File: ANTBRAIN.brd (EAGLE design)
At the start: 40 x 40 mm, 26 parts, among them IC1 ATMEGA328P, SW1 SWITCH-SPDTB

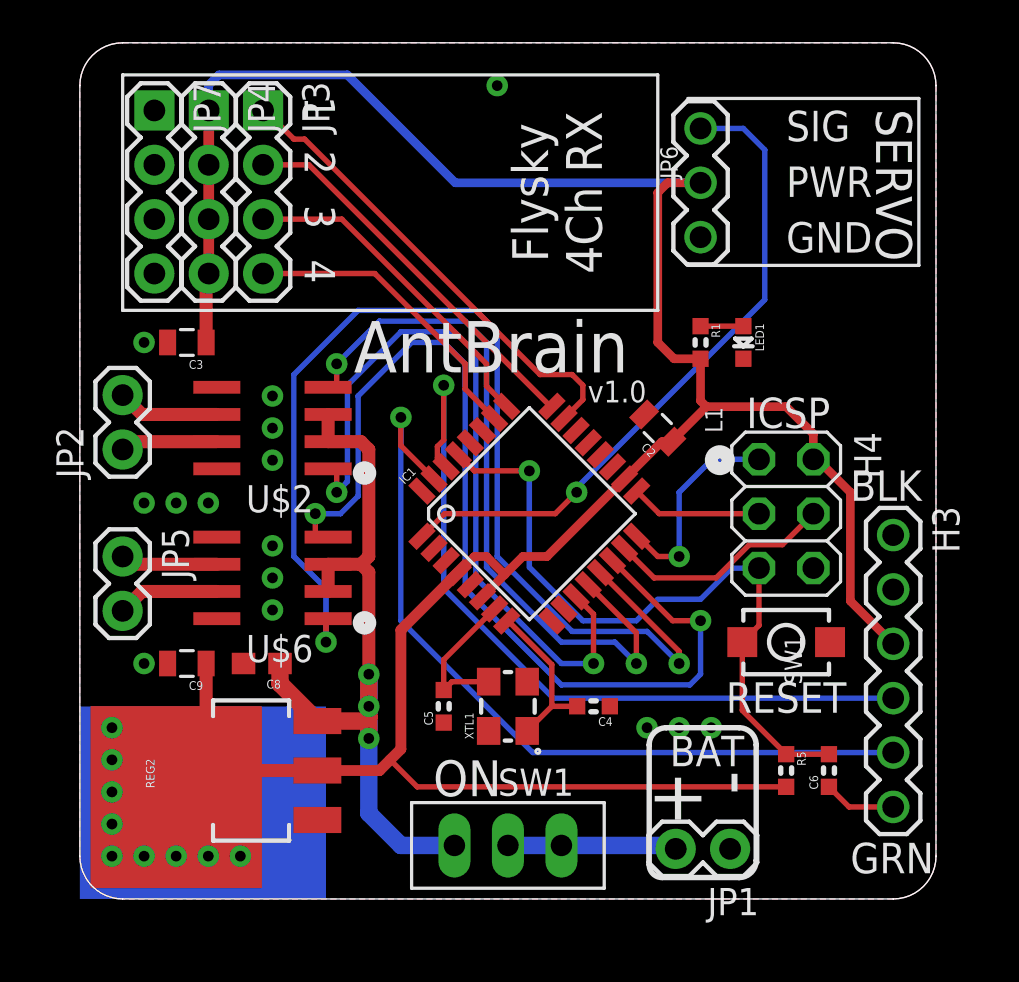
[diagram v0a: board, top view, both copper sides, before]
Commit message: Shrunk board to 36x36mm
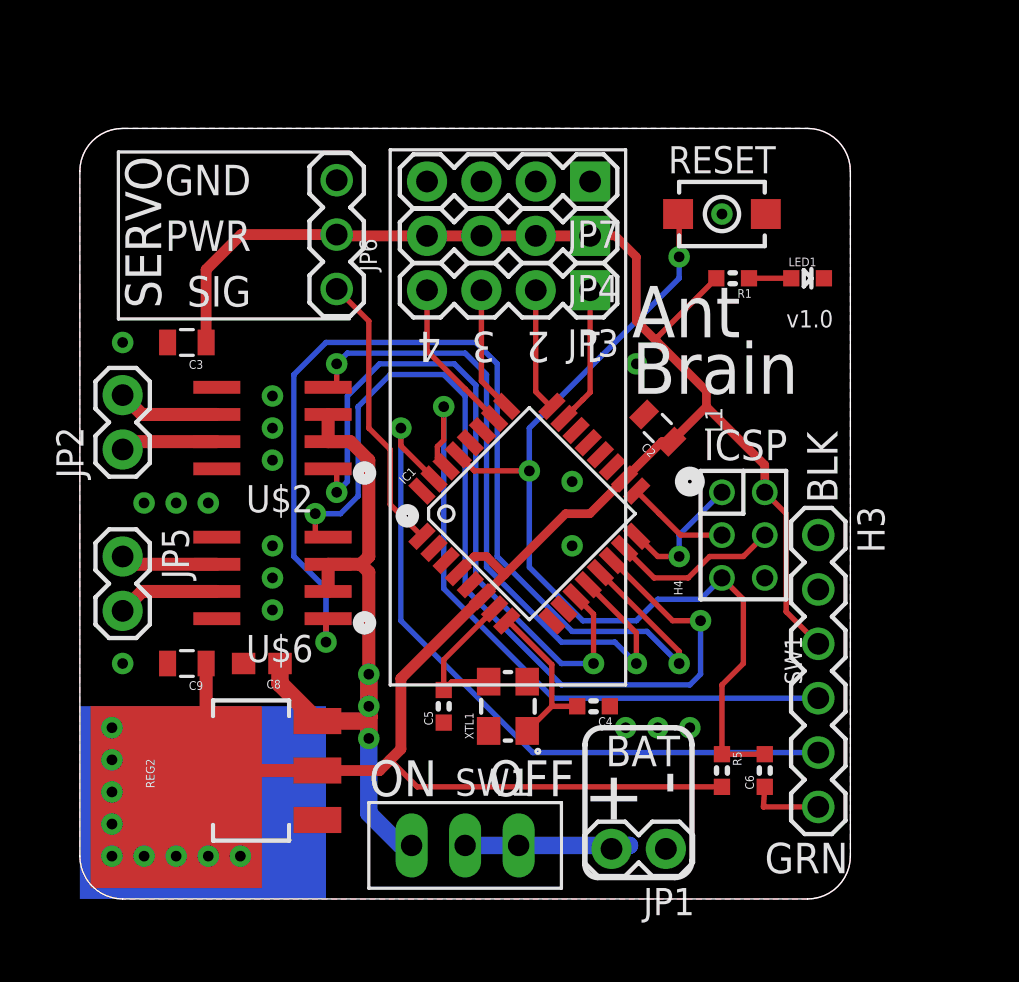
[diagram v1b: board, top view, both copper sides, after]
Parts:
- H4: value ICSP -> ICSP2X3-2MM; device pinhead:2X03 -> freetronics-jon:M2X3-2MM
- moved JP7 20.6 mm to (23.8, 33.5), turned to 180 degrees
- moved S1 20.2 mm to (30.0, 32.0)
- moved JP4 18.8 mm to (23.8, 31.0), turned to 180 degrees
- moved JP6 18.6 mm to (12.0, 28.5), turned to 90 degrees
- moved JP3 17.4 mm to (23.8, 28.4), turned to 180 degrees
- moved LED1 4.24 mm to (34.0, 29.0), turned to 0 degrees
- moved H3 3.50 mm to (34.5, 17.0)
- moved R1 3.35 mm to (30.5, 29.0), turned to 180 degrees
- moved C6 3.00 mm to (32.0, 6.00)
- moved JP1 3.00 mm to (27.4, 2.34)
- moved R5 3.00 mm to (30.0, 6.00)
- moved H4 2.24 mm to (31.0, 17.0), turned to 90 degrees
- moved SW1 2.00 mm to (18.0, 2.50)
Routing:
- net 5V: track 145.1 -> 123.7 mm
- net D3: track 31.4 -> 13.2 mm, vias 1 -> 0
- net A0: track 22.2 -> 6.60 mm
- net A1: track 18.2 -> 5.78 mm
- net RESET: track 32.8 -> 45.0 mm, vias 1 -> 2
- net A2: track 15.6 -> 5.92 mm
- net A3: track 14.3 -> 7.30 mm
- net D0_RX: track 36.7 -> 31.2 mm
- net D1_TX: track 38.6 -> 34.1 mm
- net D12_MISO: track 9.74 -> 6.20 mm
- net D11_MOSI: track 10.6 -> 7.95 mm
- net D7: track 35.4 -> 33.0 mm
- net D10: track 46.4 -> 44.0 mm
- net VBAT: track 37.7 -> 35.4 mm
- net D9: track 52.5 -> 50.3 mm
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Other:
- board size 40 x 40 mm -> 36 x 36 mm
- board text added: "Ant Brain"
- board text added: "OFF"
- board text removed: "Flysky 4Ch RX"

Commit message: Finished routing for v1.0 release
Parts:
- removed U$2, U$6: L9110SO8, freetronics-jon:SO08
- added IC2, IC3: L9110SO8, freetronics-jon:SO08
- added JP10: POWER, freetronics-jon:M02-2MM
- added JP8: (no value), freetronics-jon:M02-2MM
- added JP9: D13, freetronics-jon:M02-2MM
- added LED2: RED, freetronics-jon:LED-0603
- added R2, R3: 10K, freetronics-jon:0603
- added R4: 1K, freetronics-jon:0603
- added R6, R7: 470R, freetronics-jon:0603
- moved LED1 28.4 mm to (6.00, 33.5), turned to 90 degrees
- moved JP1 28.2 mm to (33.7, 29.9), turned to 270 degrees
- moved S1 27.0 mm to (3.00, 31.5), turned to 90 degrees
- moved R5 26.6 mm to (24.5, 32.0), turned to 0 degrees
- moved C6 25.6 mm to (24.5, 30.5), turned to 180 degrees
- moved C2 25.0 mm to (2.50, 27.0), turned to 180 degrees
- moved R1 24.5 mm to (6.00, 30.0), turned to 270 degrees
- moved JP7 23.5 mm to (2.48, 23.8), turned to 270 degrees
- moved H3 23.4 mm to (19.0, 34.5), turned to 0 degrees
- moved SW1 23.4 mm to (33.5, 20.0), turned to 270 degrees
- moved JP2 23.0 mm to (15.0, 2.00), turned to 180 degrees
- moved JP5 22.8 mm to (20.0, 2.00), turned to 0 degrees
- moved REG2 22.1 mm to (30.0, 8.00), turned to 180 degrees
- moved C3 22.0 mm to (9.50, 4.50), turned to 270 degrees
- moved C9 21.5 mm to (25.5, 4.50), turned to 90 degrees
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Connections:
- removed net N$1: JP2.1, U$2.7
- removed net N$2: JP2.2, U$2.6
- removed net N$3: JP5.2, U$6.7
- removed net N$4: JP5.1, U$6.6
- new net LA: IC2.6, JP2.2
- new net LB: IC2.7, JP2.1
- new net N$5: LED2.A, R4.1
- new net N$6: JP10.1, R7.1
- new net N$8: JP9.1, R6.1
- new net RA: IC3.6, JP5.1
- new net RB: IC3.7, JP5.2
- net 5V: now also R7.2
- net A6: now also R2.2, R3.1
- net D10: now also IC3.4; no longer U$6.4
- net D13_SCK: now also R4.2, R6.2
- net D7: now also IC2.1; no longer U$2.1
- net D8: now also IC2.4; no longer U$2.4
- net D9: now also IC3.1; no longer U$6.1
- net GND: now also IC2.5, IC2.8, IC3.5, IC3.8, JP10.2, JP9.2, LED2.C, R2.1; no longer U$2.5, U$2.8, U$6.5, U$6.8
- net N$9: now also JP8.2
- net VBAT: now also IC2.2, IC2.3, IC3.2, IC3.3, JP8.1, R3.2; no longer U$2.2, U$2.3, U$6.2, U$6.3
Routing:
- net A6: track 0.00 -> 55.4 mm, vias 0 -> 2
- net D13_SCK: track 4.84 -> 22.5 mm, vias 0 -> 2
- net VBAT: track 35.4 -> 48.7 mm
- net RTS: track 3.50 -> 9.60 mm
- net N$3: track 4.77 -> 0.00 mm
- net LA: track 0.00 -> 4.77 mm
- net RB: track 0.00 -> 4.77 mm
- net N$2: track 4.77 -> 0.00 mm
- net N$4: track 4.55 -> 0.00 mm
- net LB: track 0.00 -> 4.55 mm
- net RA: track 0.00 -> 4.55 mm
- net N$1: track 4.55 -> 0.00 mm
- net 5V: track 123.7 -> 120.2 mm
- net N$9: track 8.54 -> 10.5 mm
- net N$5: track 0.00 -> 1.98 mm
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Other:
- board text added: "BK"
- board text added: "D13"
- board text added: "LA"
- board text added: "LB"
- board text added: "RA"
- board text added: "RB"
- board text added: "SWITCH"
- board text added: "freetronics"
- board text removed: "Ant Brain"
- board text removed: "BLK"
- board text removed: "OFF"

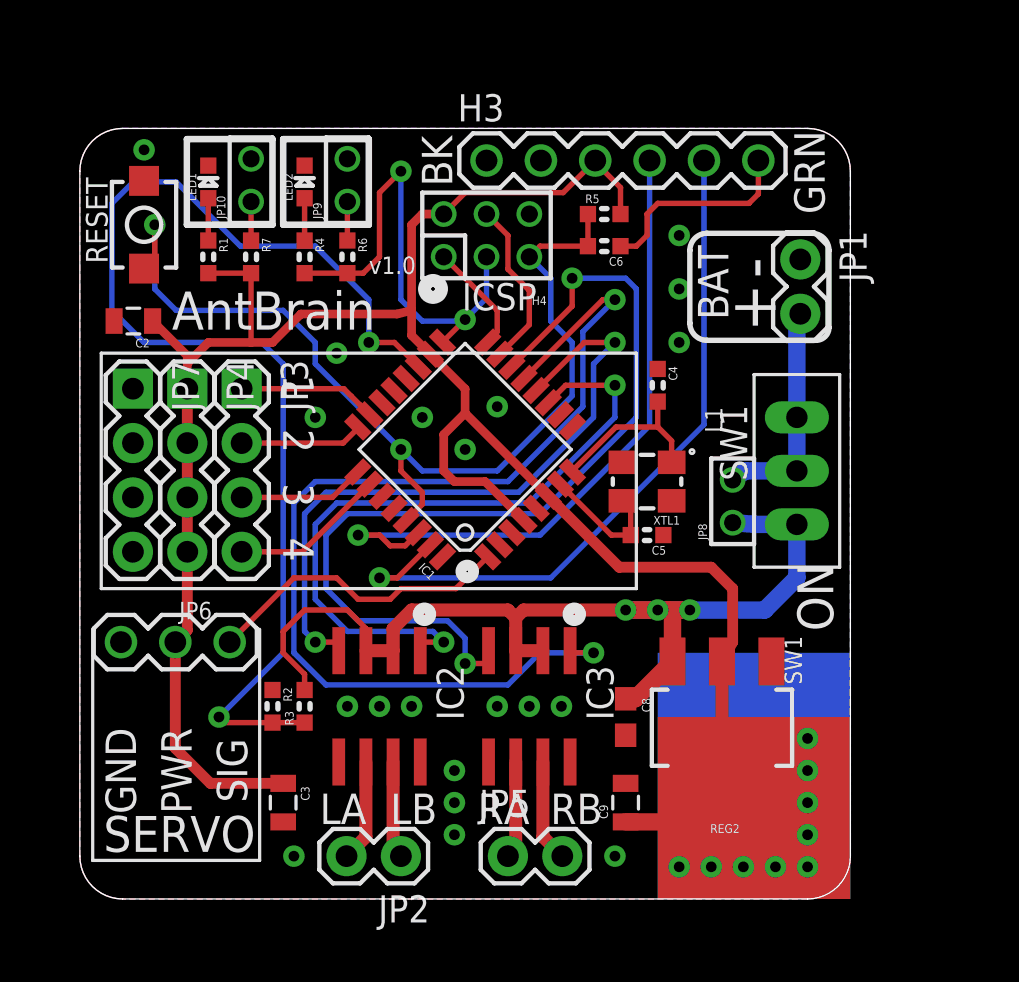
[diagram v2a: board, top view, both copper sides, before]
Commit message: Fixed H-Bridge footprints for v1.1 release
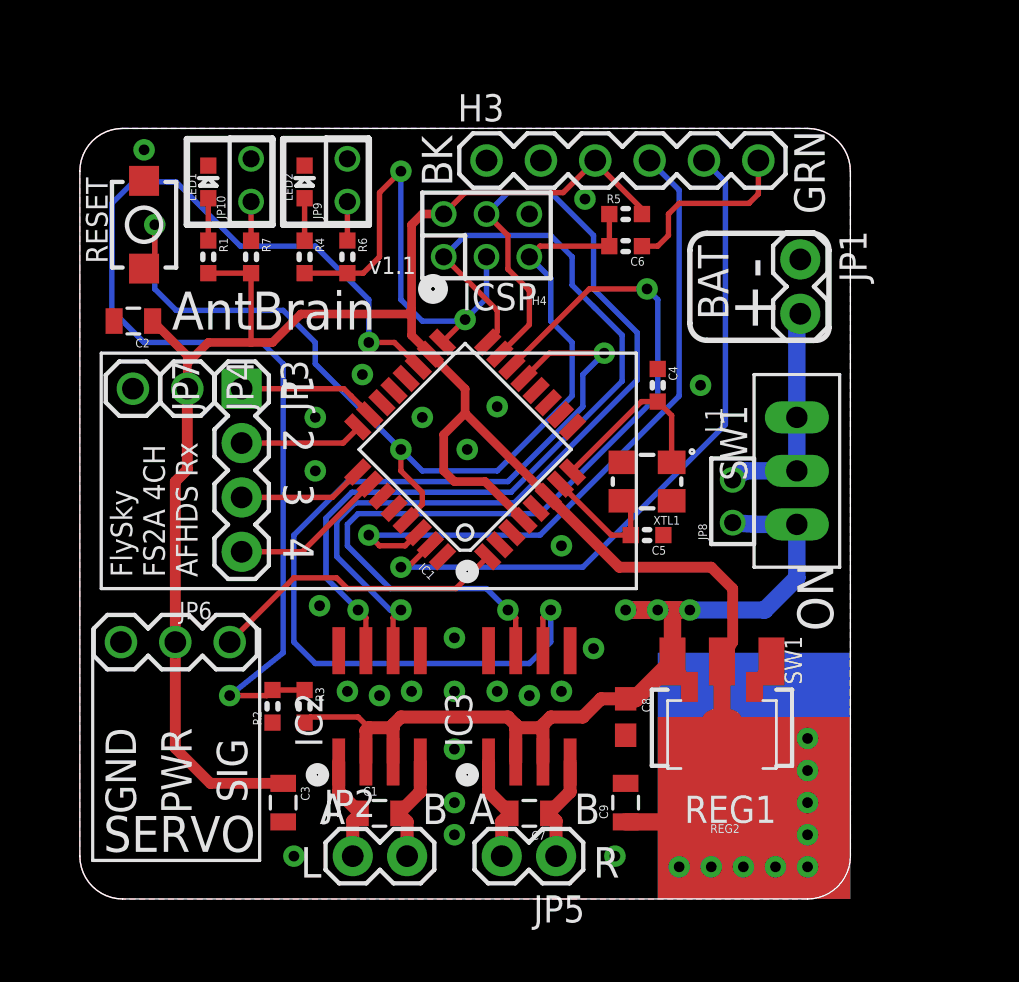
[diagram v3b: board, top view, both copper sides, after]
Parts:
- added C1, C7: 10uF, freetronics-jon:0805
- added REG1: LD1117-SOT89, freetronics:SOT89
- JP4, JP7: value (none) -> M01PTH; device freetronics-jon:1X04 -> freetronics-jon:1X01
- moved JP2 2.25 mm to (12.8, 2.00), turned to 0 degrees
- moved JP5 2.25 mm to (22.2, 2.00), turned to 180 degrees
- moved C6 1.00 mm to (25.5, 30.5)
- moved R5 1.00 mm to (25.5, 32.0)
- turned IC2 to 0 degrees
- turned IC3 to 0 degrees
- turned R2 to 90 degrees
- turned R3 to 270 degrees
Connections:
- removed net LA: IC2.6, JP2.2
- removed net LB: IC2.7, JP2.1
- removed net RA: IC3.6, JP5.1
- removed net RB: IC3.7, JP5.2
- new net LOA: C1.1, IC2.1, JP2.1
- new net LOB: C1.2, IC2.4, JP2.2
- new net ROA: C7.2, IC3.1, JP5.2
- new net ROB: C7.1, IC3.4, JP5.1
- net 5V: now also REG1.2, REG1.4; no longer JP4.2, JP4.3, JP4.4
- net D10: now also IC3.7; no longer IC3.4
- net D11_MOSI: now also IC2.6
- net D12_MISO: now also IC2.7
- net D7: no longer IC2.1
- net D8: no longer IC2.4
- net D9: now also IC3.6; no longer IC3.1
- net GND: now also REG1.1; no longer JP7.2, JP7.3, JP7.4
- net VBAT: now also REG1.3
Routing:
- net D11_MOSI: track 7.95 -> 46.3 mm, vias 0 -> 1
- net D12_MISO: track 5.20 -> 42.3 mm, vias 0 -> 1
- net D7: track 33.0 -> 0.00 mm, vias 2 -> 0
- net D8: track 31.5 -> 0.00 mm, vias 2 -> 0
- net D9: track 50.3 -> 44.5 mm
- net ROA: track 0.00 -> 4.98 mm
- net LOB: track 0.00 -> 4.98 mm
- net ROB: track 0.00 -> 4.96 mm
- net LOA: track 0.00 -> 4.96 mm
- net LA: track 4.77 -> 0.00 mm
- net RB: track 4.77 -> 0.00 mm
- net LB: track 4.55 -> 0.00 mm
- net RA: track 4.55 -> 0.00 mm
- net D10: track 44.0 -> 41.8 mm
- net 5V: track 120.2 -> 122.0 mm
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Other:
- board text added: "5V FTDI"
- board text added: "7.4V LiPo"
- board text added: "A"
- board text added: "A0: CH1 A1: CH2 A2: CH3 A3: CH4 A6: VBAT"
- board text added: "ATmega328P 16MHz"
- board text added: "B"
- board text added: "D11: LA D12: LB D9: RA D10: RB D13: LED"
- board text added: "FlySky FS2A 4CH AFHDS Rx"
- board text added: "L"
- board text added: "R"
- board text added: "Select "Arduino Uno" in Arduino IDE"
- board text added: "v1.1"
- board text removed: "LA"
- board text removed: "LB"
- board text removed: "RA"
- board text removed: "RB"
- board text removed: "v1.0"
